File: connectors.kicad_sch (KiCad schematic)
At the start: 2 parts, among them J1 CM4_Plug_Module_Hirose_DF40_2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

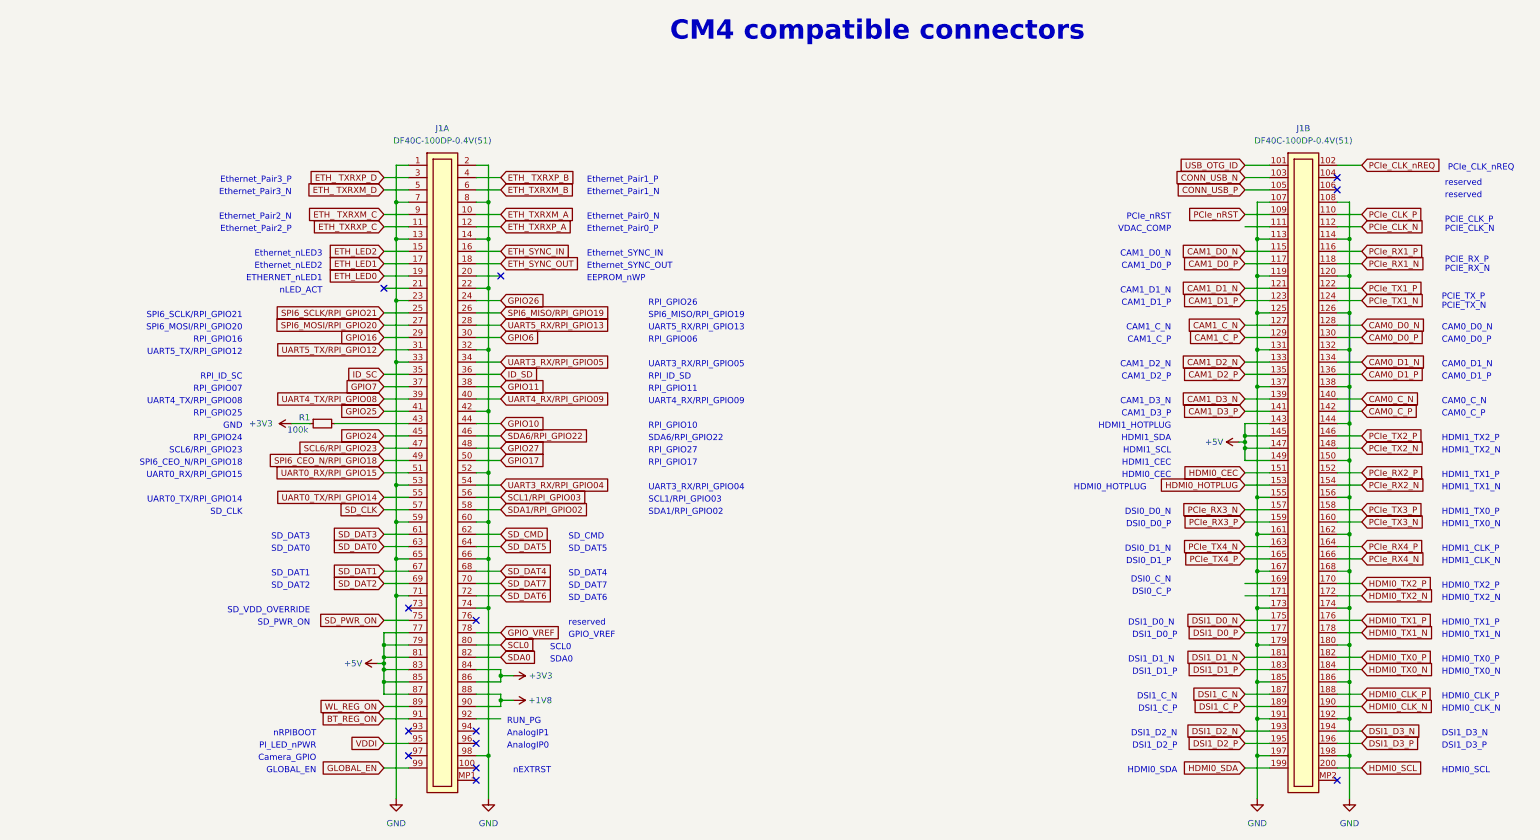
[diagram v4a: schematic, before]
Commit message: [#54899] Flag not connected pins
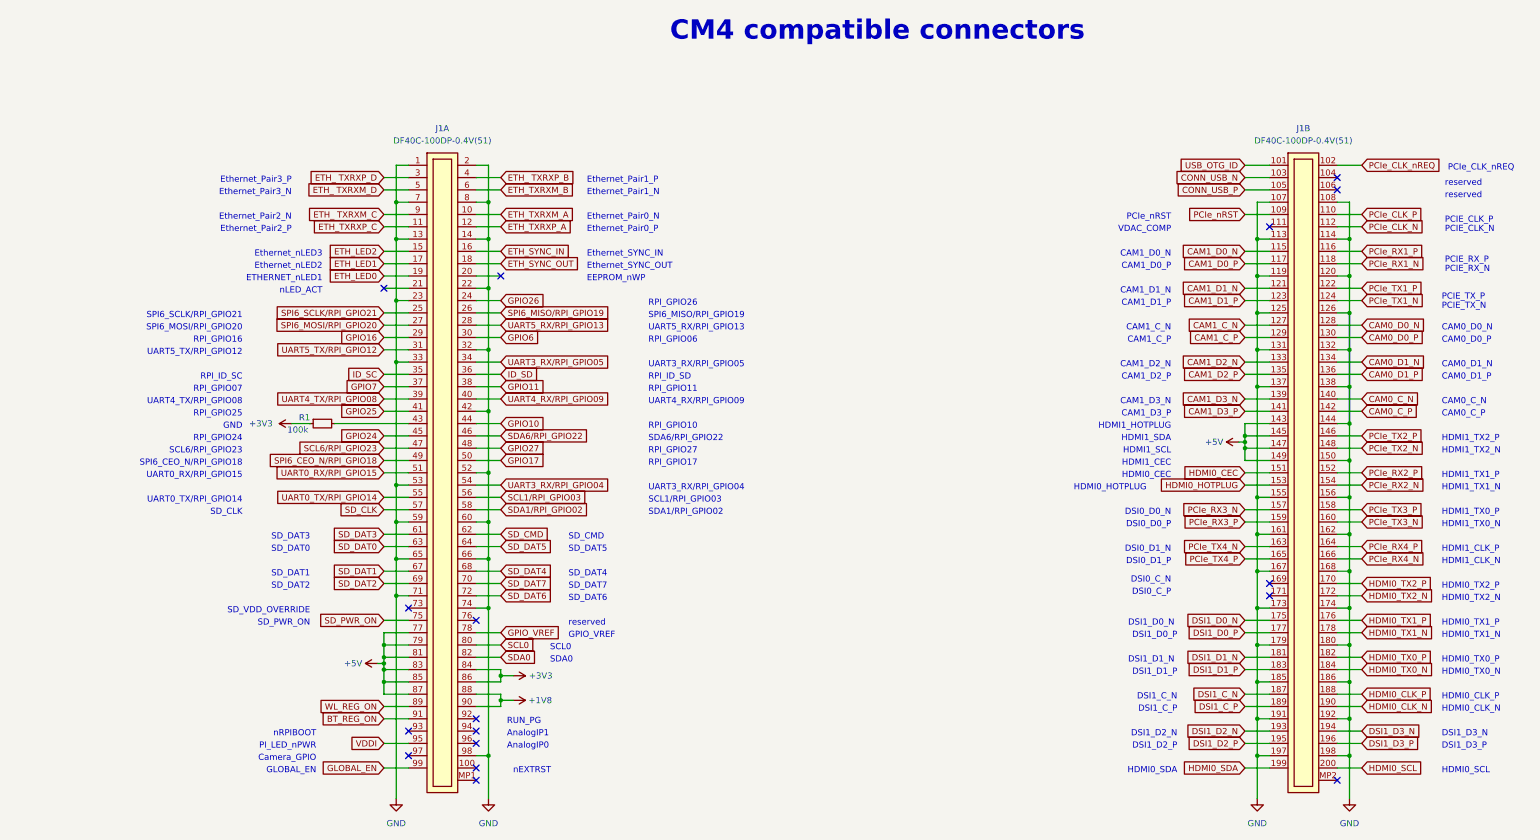
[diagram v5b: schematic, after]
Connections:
- no-connect marks 13 -> 17
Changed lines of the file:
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@@
   (no_connect (at 110.49 170.18))
   (no_connect (at 124.46 205.74))
+  (no_connect (at 288.29 167.64))
+  (no_connect (at 288.29 165.1))
   (no_connect (at 124.46 195.58))
   (no_connect (at 110.49 200.66))
@@
   (no_connect (at 302.26 205.74))
   (no_connect (at 124.46 198.12))
+  (no_connect (at 124.46 193.04))
   (no_connect (at 110.49 195.58))
   (no_connect (at 129.54 101.6))
+  (no_connect (at 288.29 91.44))
   (no_connect (at 302.26 81.28))
   (wire (pts (xy 302.26 180.34) (xy 307.34 180.34))
@@
     (stroke (width 0) (type default))
   )
-  (wire (pts (xy 283.21 91.44) (xy 288.29 91.44))
-    (stroke (width 0) (type default))
-  )
   (wire (pts (xy 304.8 132.08) (xy 304.8 139.7))
     (stroke (width 0) (type default))
@@
     (stroke (width 0) (type default))
   )
-  (wire (pts (xy 283.21 165.1) (xy 288.29 165.1))
-    (stroke (width 0) (type default))
-  )
   (wire (pts (xy 285.75 185.42) (xy 285.75 193.04))
     (stroke (width 0) (type default))
@@
     (stroke (width 0) (type default))
   )
-  (wire (pts (xy 124.46 193.04) (xy 129.54 193.04))
-    (stroke (width 0) (type default))
-  )
   (wire (pts (xy 124.46 170.18) (xy 127 170.18))
     (stroke (width 0) (type default))
@@
     (stroke (width 0) (type default))
   )
-  (wire (pts (xy 283.21 167.64) (xy 288.29 167.64))
-    (stroke (width 0) (type default))
-  )

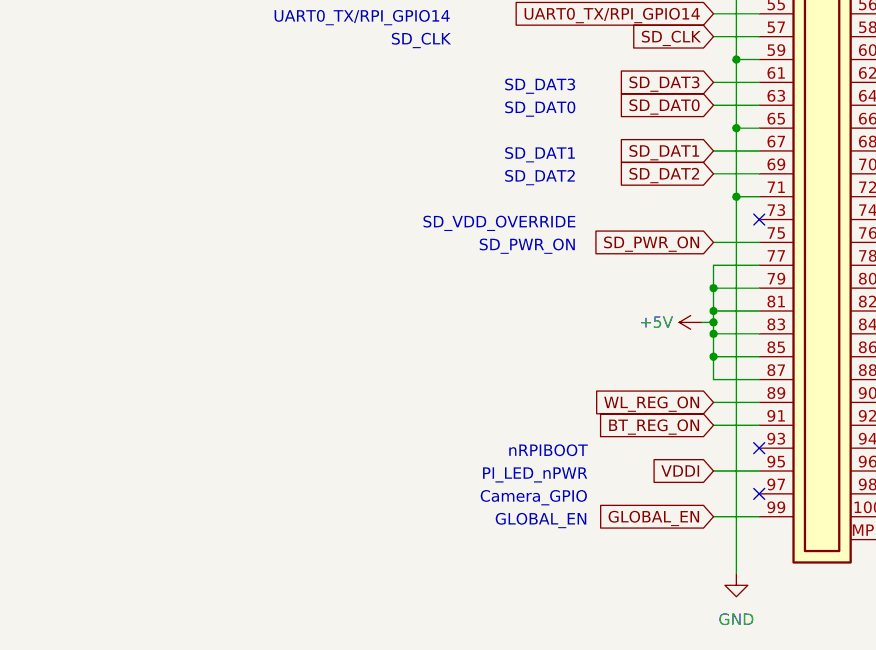
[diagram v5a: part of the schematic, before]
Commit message: [#54899] Add ideal diode on HDMI1 5V input
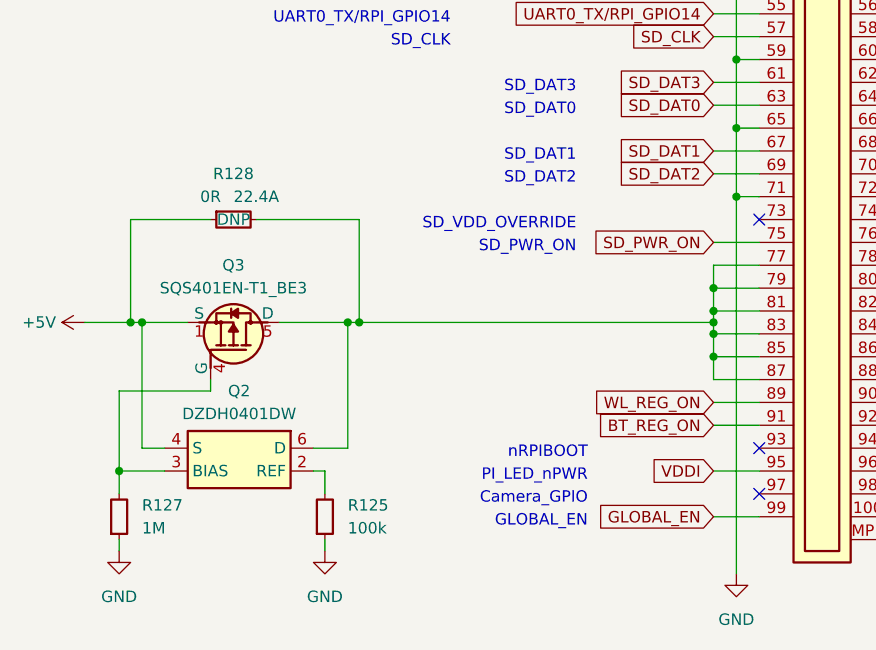
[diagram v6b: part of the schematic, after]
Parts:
- added Q2: DZDH0401DW, antmicro-footprints:SOT-363, symbol antmicroPMICORControllersIdealDiodes:DZDH0401DW
- added Q3: SQS401EN-T1_BE3, antmicro-footprints:Vishay_PowerPAK_1212-8_Single, symbol antmicroTransistorsFETsMOSFETsSingle:SQS401EN-T1_BE3
- added R125: R_100k_0402, antmicro-footprints:R_0402_1005Metric, symbol antmicroResistors0402:R_100k_0402
- added R127: R_1M_0402, antmicro-footprints:R_0402_1005Metric, symbol antmicroResistors0402:R_1M_0402
- added R128: R_0R_22.4A_0603, antmicro-footprints:R_0603_1608Metric, symbol antmicroResistors0603:R_0R_22.4A_0603
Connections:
- net +5V: now also Q2.4 (S), Q3.1 (S), Q3.2 (S), Q3.3 (S), R128.1; no longer J1.77, J1.79, J1.81, J1.83, J1.85, J1.87
- net GND: now also R125.1, R127.1
- new net: Q2.3 (BIAS), Q3.4 (G), R127.2
- new net: Q2.2 (REF), R125.2
- new net: J1.77, J1.79, J1.81, J1.83, J1.85, J1.87, Q2.6 (D), Q3.5 (D), R128.2

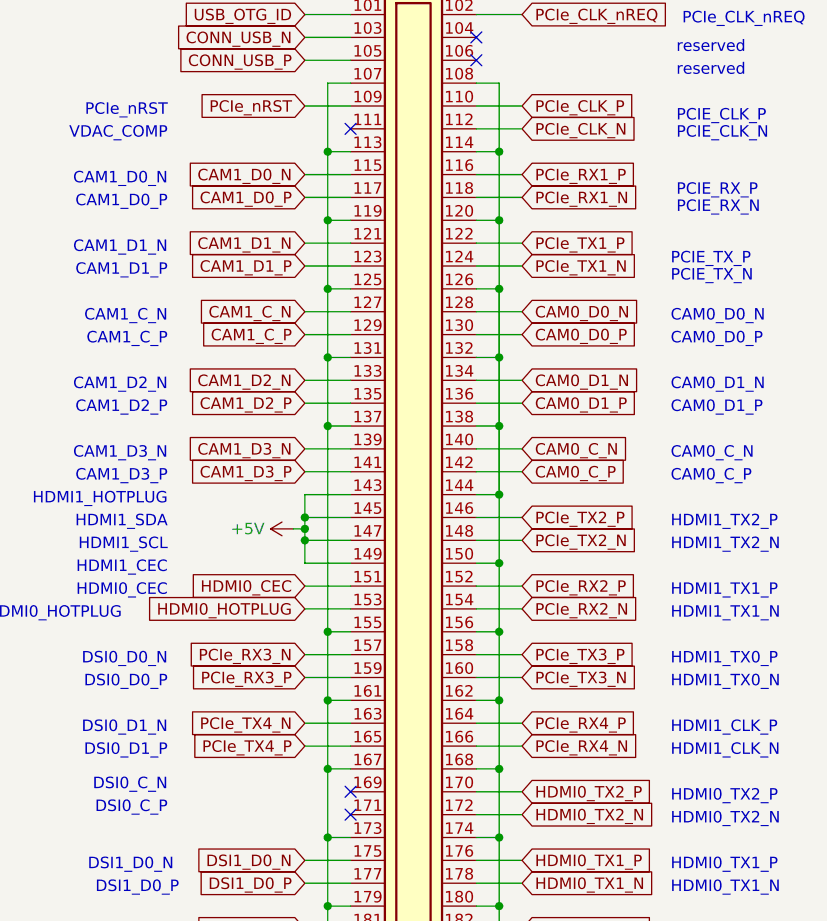
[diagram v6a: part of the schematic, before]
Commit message: [#54899] Rename PCIe connections
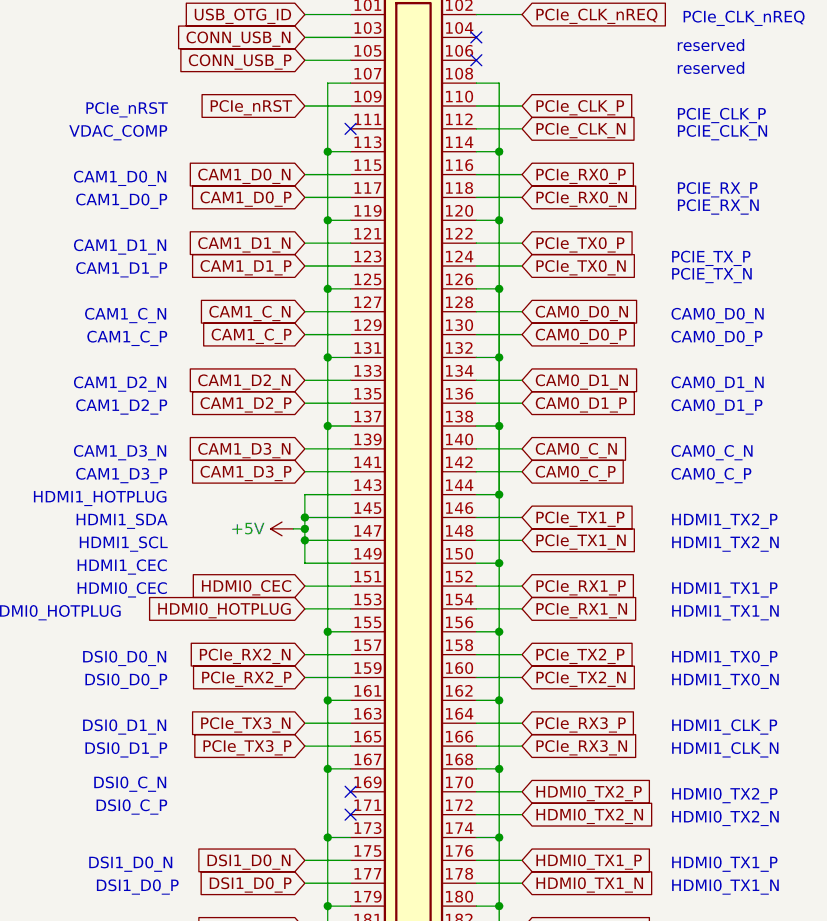
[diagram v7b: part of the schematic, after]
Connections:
- net PCIe_RX4_N is gone; now on net PCIe_RX3_N: J1.166
- net PCIe_RX4_P is gone; now on net PCIe_RX3_P: J1.164
- net PCIe_TX4_N is gone; now on net PCIe_TX3_N: J1.163
- net PCIe_TX4_P is gone; now on net PCIe_TX3_P: J1.165
- net PCIe_RX1_N: now also J1.154; no longer J1.118
- net PCIe_RX1_P: now also J1.152; no longer J1.116
- net PCIe_RX2_N: now also J1.157; no longer J1.154
- net PCIe_RX2_P: now also J1.159; no longer J1.152
- net PCIe_RX3_N: no longer J1.157
- net PCIe_RX3_P: no longer J1.159
- net PCIe_TX1_N: now also J1.148; no longer J1.124
- net PCIe_TX1_P: now also J1.146; no longer J1.122
- net PCIe_TX2_N: now also J1.160; no longer J1.148
- net PCIe_TX2_P: now also J1.158; no longer J1.146
- net PCIe_TX3_N: no longer J1.160
- net PCIe_TX3_P: no longer J1.158
- new net PCIe_RX0_N: J1.118
- new net PCIe_RX0_P: J1.116
- new net PCIe_TX0_N: J1.124
- new net PCIe_TX0_P: J1.122

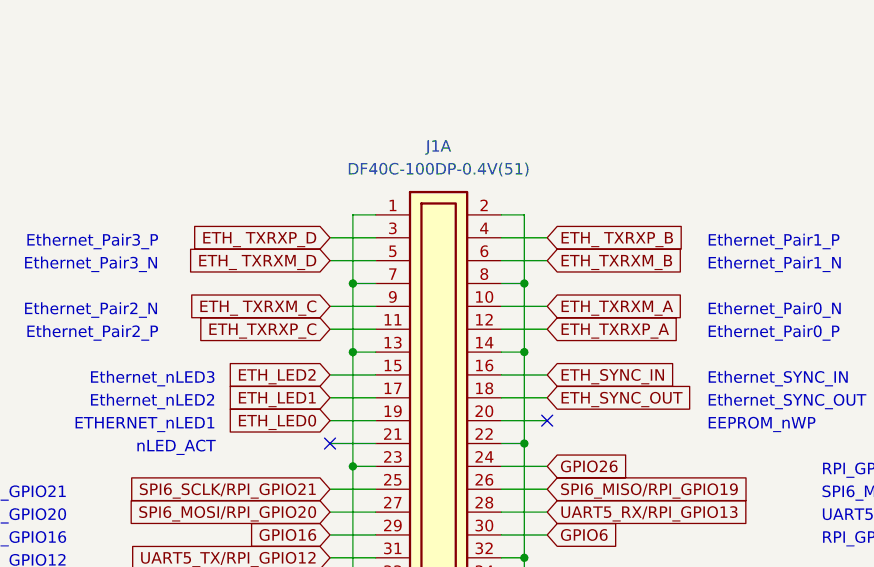
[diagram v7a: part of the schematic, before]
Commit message: [#54899] Change ETH labels to differential
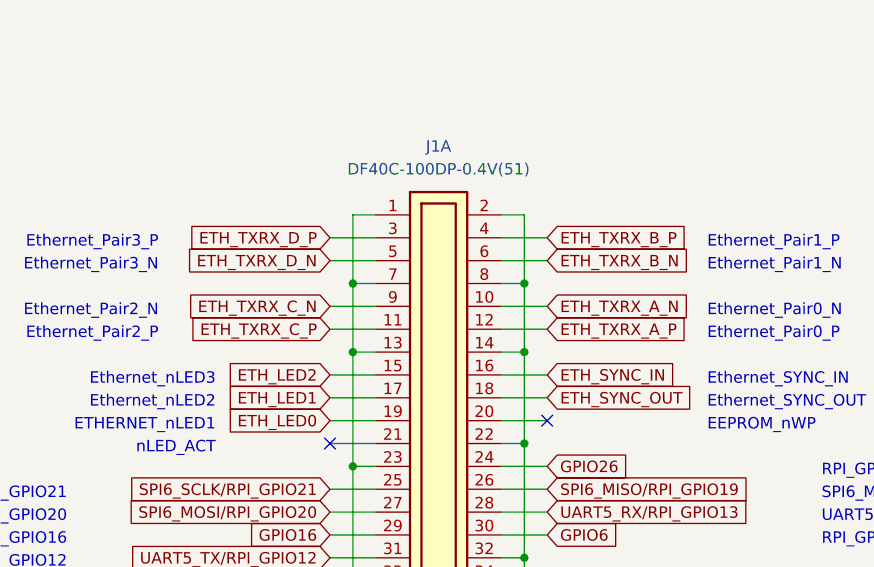
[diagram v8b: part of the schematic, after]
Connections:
- net ETH_ TXRXM_C renamed ETH_TXRX_C_N
- net ETH_ TXRXM_D renamed ETH_TXRX_D_N
- net ETH_ TXRXP_B renamed ETH_TXRX_B_P
- net ETH_ TXRXP_D renamed ETH_TXRX_D_P
- net ETH_TXRXM_A renamed ETH_TXRX_A_N
- net ETH_TXRXM_B renamed ETH_TXRX_B_N
- net ETH_TXRXP_A renamed ETH_TXRX_A_P
- net ETH_TXRXP_C renamed ETH_TXRX_C_P
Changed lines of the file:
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@@
+    )
+  )
+  (global_label "ETH_TXRX_D_N" (shape input) (at 105.41 83.82 180) (fields_autoplaced)
+    (effects (font (size 1.27 1.27)) (justify right))
+    (property "Intersheetrefs" "${INTERSHEET_REFS}" (at 88.8178 83.82 0)
+      (effects (font (size 1.27 1.27)) (justify right) hide)
     )
   )
@@
     )
   )
+  (global_label "ETH_TXRX_B_P" (shape input) (at 129.54 81.28 0) (fields_autoplaced)
+    (effects (font (size 1.27 1.27)) (justify left))
+    (property "Intersheetrefs" "${INTERSHEET_REFS}" (at 146.0717 81.28 0)
+      (effects (font (size 1.27 1.27)) (justify left) hide)
+    )
+  )
   (global_label "SD_CMD" (shape input) (at 129.54 154.94 0) (fields_autoplaced)
     (effects (font (size 1.27 1.27)) (justify left))
@@
     )
   )
-  (global_label "ETH_TXRXM_B" (shape input) (at 129.54 83.82 0) (fields_autoplaced)
-    (effects (font (size 1.27 1.27)) (justify left))
-    (property "Intersheetrefs" "${INTERSHEET_REFS}" (at 144.7136 83.7406 0)
-      (effects (font (size 1.27 1.27)) (justify left) hide)
-    )
-  )
   (global_label "CONN_USB_N" (shape input) (at 283.21 81.28 180) (fields_autoplaced)
     (effects (font (size 1.27 1.27)) (justify right))
@@
     )
   )
+  (global_label "ETH_TXRX_C_N" (shape input) (at 105.41 88.9 180) (fields_autoplaced)
+    (effects (font (size 1.27 1.27)) (justify right))
+    (property "Intersheetrefs" "${INTERSHEET_REFS}" (at 88.8178 88.9 0)
+      (effects (font (size 1.27 1.27)) (justify right) hide)
+    )
+  )
   (global_label "DSI1_D3_N" (shape input) (at 307.34 195.58 0) (fields_autoplaced)
     (effects (font (size 1.27 1.27)) (justify left))
@@
     )
   )
+  (global_label "ETH_TXRX_A_N" (shape input) (at 129.54 88.9 0) (fields_autoplaced)
+    (effects (font (size 1.27 1.27)) (justify left))
+    (property "Intersheetrefs" "${INTERSHEET_REFS}" (at 145.9508 88.9 0)
+      (effects (font (size 1.27 1.27)) (justify left) hide)
+    )
+  )
   (global_label "DSI1_D2_P" (shape input) (at 283.21 198.12 180) (fields_autoplaced)
     (effects (font (size 1.27 1.27)) (justify right))
@@
     )
   )
-  (global_label "ETH_TXRXM_A" (shape input) (at 129.54 88.9 0) (fields_autoplaced)
-    (effects (font (size 1.27 1.27)) (justify left))
-    (property "Intersheetrefs" "${INTERSHEET_REFS}" (at 144.5321 88.8206 0)
-      (effects (font (size 1.27 1.27)) (justify left) hide)
-    )
-  )
   (global_label "SCL6{slash}RPI_GPIO23" (shape input) (at 105.41 137.16 180) (fields_autoplaced)
     (effects (font (size 1.27 1.27)) (justify right))
@@
     )
   )
-  (global_label "ETH_TXRXP_C" (shape input) (at 105.41 91.44 180) (fields_autoplaced)
-    (effects (font (size 1.27 1.27)) (justify right))
-    (property "Intersheetrefs" "${INTERSHEET_REFS}" (at 90.4179 91.3606 0)
-      (effects (font (size 1.27 1.27)) (justify right) hide)
-    )
-  )
   (global_label "PCIe_RX2_P" (shape input) (at 283.21 152.4 180) (fields_autoplaced)
     (effects (font (size 1.27 1.27)) (justify right))
@@
     )
   )
-  (global_label "ETH_ TXRXP_D" (shape input) (at 105.41 81.28 180) (fields_autoplaced)
-    (effects (font (size 1.27 1.27)) (justify right))
-    (property "Intersheetrefs" "${INTERSHEET_REFS}" (at 89.4502 81.2006 0)
-      (effects (font (size 1.27 1.27)) (justify right) hide)
-    )
-  )
   (global_label "GPIO25" (shape input) (at 105.41 129.54 180) (fields_autoplaced)
     (effects (font (size 1.27 1.27)) (justify right))
@@
     )
   )
-  (global_label "ETH_ TXRXM_D" (shape input) (at 105.41 83.82 180) (fields_autoplaced)
-    (effects (font (size 1.27 1.27)) (justify right))
-    (property "Intersheetrefs" "${INTERSHEET_REFS}" (at 89.2688 83.7406 0)
+  (global_label "ETH_TXRX_D_P" (shape input) (at 105.41 81.28 180) (fields_autoplaced)
+    (effects (font (size 1.27 1.27)) (justify right))
+    (property "Intersheetrefs" "${INTERSHEET_REFS}" (at 88.8783 81.28 0)
       (effects (font (size 1.27 1.27)) (justify right) hide)
     )
@@
     )
   )
+  (global_label "ETH_TXRX_A_P" (shape input) (at 129.54 91.44 0) (fields_autoplaced)
+    (effects (font (size 1.27 1.27)) (justify left))
+    (property "Intersheetrefs" "${INTERSHEET_REFS}" (at 145.8903 91.44 0)
+      (effects (font (size 1.27 1.27)) (justify left) hide)
+    )
+  )
   (global_label "CAM0_D1_P" (shape input) (at 307.34 121.92 0) (fields_autoplaced)
     (effects (font (size 1.27 1.27)) (justify left))
@@
     )
   )
-  (global_label "ETH_TXRXP_A" (shape input) (at 129.54 91.44 0) (fields_autoplaced)
-    (effects (font (size 1.27 1.27)) (justify left))
-    (property "Intersheetrefs" "${INTERSHEET_REFS}" (at 144.3507 91.3606 0)
-      (effects (font (size 1.27 1.27)) (justify left) hide)
-    )
-  )
-  (global_label "ETH_ TXRXM_C" (shape input) (at 105.41 88.9 180) (fields_autoplaced)
-    (effects (font (size 1.27 1.27)) (justify right))
-    (property "Intersheetrefs" "${INTERSHEET_REFS}" (at 89.2688 88.8206 0)
-      (effects (font (size 1.27 1.27)) (justify right) hide)
+  (global_label "ETH_TXRX_B_N" (shape input) (at 129.54 83.82 0) (fields_autoplaced)
+    (effects (font (size 1.27 1.27)) (justify left))
+    (property "Intersheetrefs" "${INTERSHEET_REFS}" (at 146.1322 83.82 0)
+      (effects (font (size 1.27 1.27)) (justify left) hide)
     )
   )
@@
     )
   )
+  (global_label "ETH_TXRX_C_P" (shape input) (at 105.41 91.44 180) (fields_autoplaced)
+    (effects (font (size 1.27 1.27)) (justify right))
+    (property "Intersheetrefs" "${INTERSHEET_REFS}" (at 88.8783 91.44 0)
+      (effects (font (size 1.27 1.27)) (justify right) hide)
+    )
+  )
   (global_label "HDMI0_TX0_P" (shape input) (at 307.34 180.34 0) (fields_autoplaced)
     (effects (font (size 1.27 1.27)) (justify left))
@@
     )
   )
-  (global_label "ETH_ TXRXP_B" (shape input) (at 129.54 81.28 0) (fields_autoplaced)
-    (effects (font (size 1.27 1.27)) (justify left))
-    (property "Intersheetrefs" "${INTERSHEET_REFS}" (at 145.4998 81.2006 0)
-      (effects (font (size 1.27 1.27)) (justify left) hide)
-    )
-  )
